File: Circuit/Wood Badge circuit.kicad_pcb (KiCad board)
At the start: 2 copper layers, 60 x 60 mm, 12 parts, among them J1 Conn_01x02_Pin, U1 LM555xN

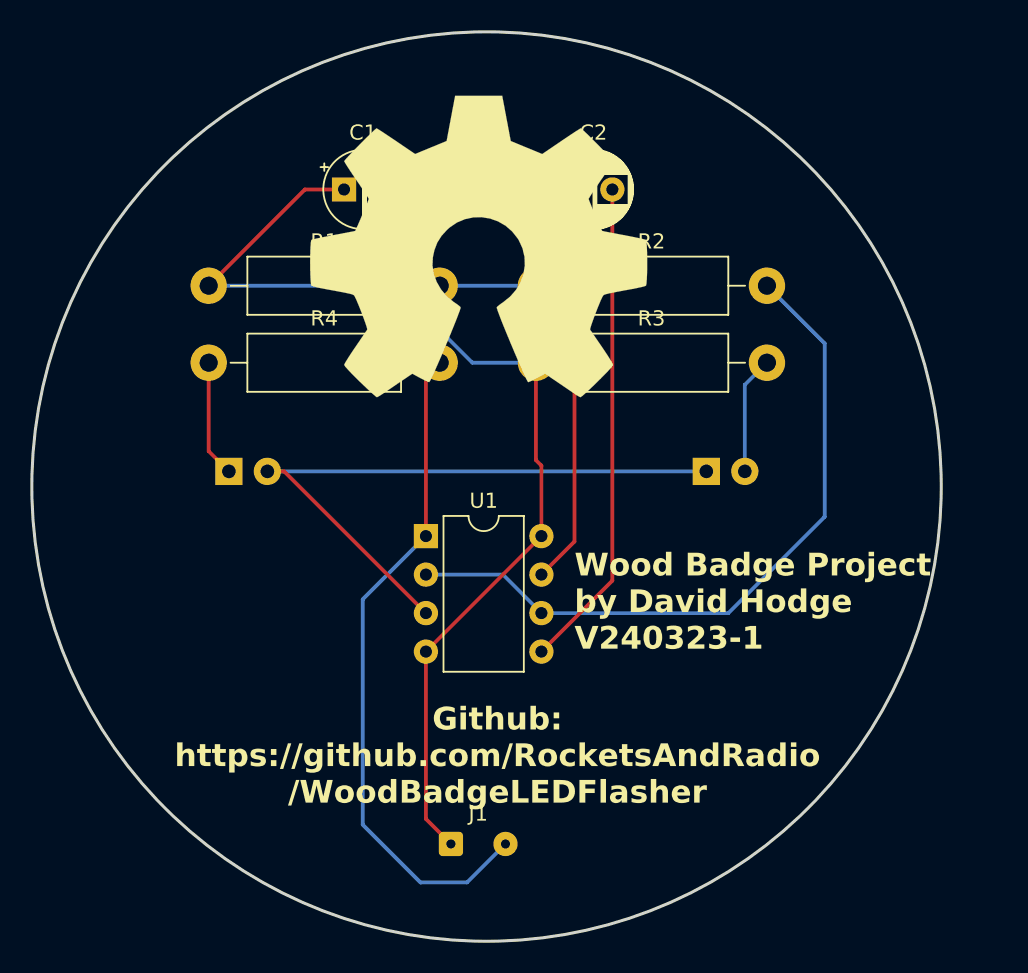
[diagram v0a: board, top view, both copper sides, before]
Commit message: Added C3 (below R1, R2 oops) Added values of components to reach a 2Hz frequency
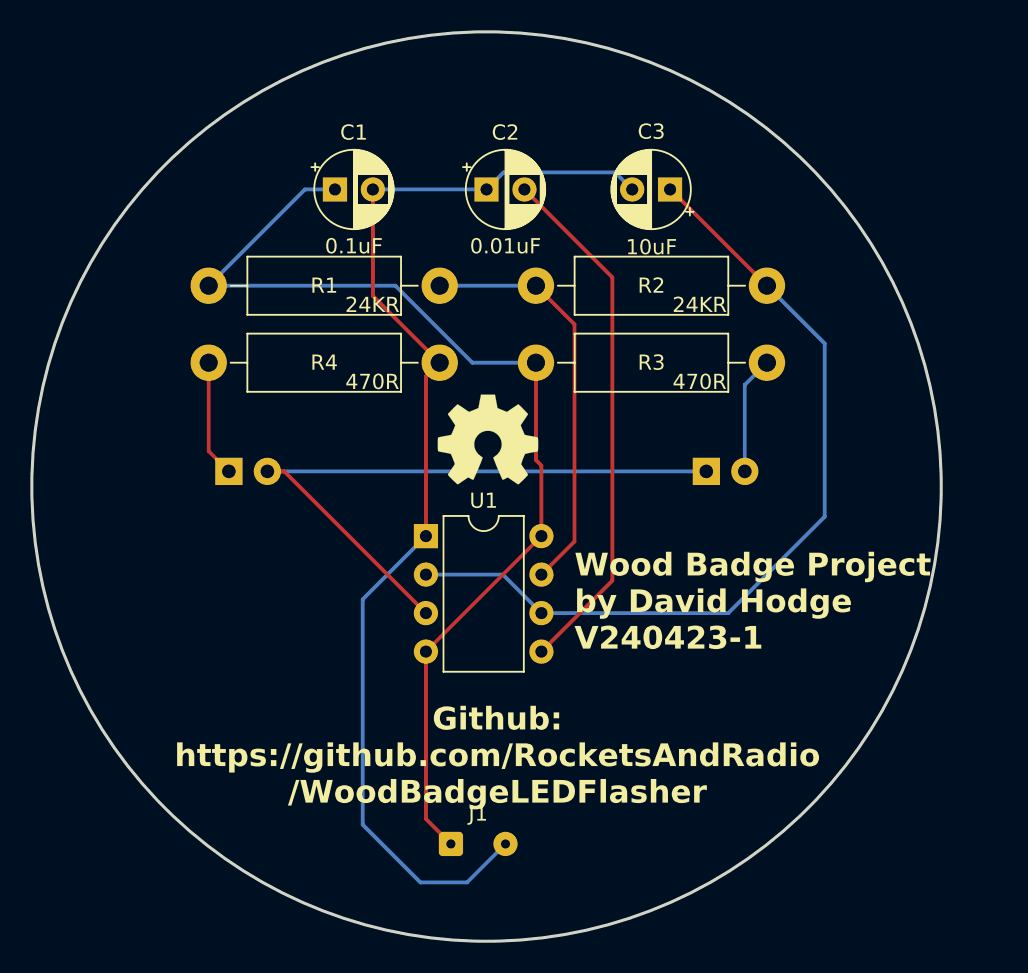
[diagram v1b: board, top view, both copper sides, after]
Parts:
- removed the REF** at (44.5, 29.2)
- added C3: 10uF, Capacitor_THT:CP_Radial_D5.0mm_P2.50mm, F.Cu at (57.1, 25.4)
- added REF**: OSHW-Symbol_6.7x6mm_SilkScreen, Symbol:OSHW-Symbol_6.7x6mm_SilkScreen, F.Cu at (45.1, 41.9)
- C1: value C_Small -> 0.1uF
- C2: value C_Small -> 0.01uF
- R1, R2: value R_US -> 24KR
- R3, R4: value R_US -> 470R
- moved C2 5.80 mm to (45.0, 25.4)
- moved C1 0.60 mm to (35.0, 25.4)
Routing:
- net /trigger-threshold: track 46.8 -> 55.8 mm
- net GND: track 70.3 -> 75.9 mm
- net Net-(U1-CV): track 32.4 -> 34.8 mm
- net VCC: track 71.0 -> 70.4 mm
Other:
- board text added: "Wood Badge Project by David Hodge V240423-1"
- board text removed: "Wood Badge Project by David Hodge V240323-1"

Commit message: Amendments to reflect fixes for faults identified in the first time the circuit was put together, such as adding capacitor C3.
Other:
- board text added: "Wood Badge Project by Kanga V240517-1"
- board text removed: "Wood Badge Project by David Hodge V240423-1"
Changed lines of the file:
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@@
 		(pad "1" thru_hole rect
 			(at 0 0)
-			(size 1.6 1.6)
+			(size 2 2.5)
 			(drill 0.8)
 			(layers "*.Cu" "*.Mask")
@@
 		(pad "2" thru_hole circle
 			(at 2.5 0)
-			(size 1.6 1.6)
+			(size 2 2)
 			(drill 0.8)
 			(layers "*.Cu" "*.Mask")
@@
 		(pad "1" thru_hole rect
 			(at 0 0)
-			(size 1.6 1.6)
+			(size 2.5 2)
 			(drill 0.8)
 			(layers "*.Cu" "*.Mask")
@@
 		(pad "2" thru_hole oval
 			(at 0 2.54)
-			(size 1.6 1.6)
+			(size 2 2)
 			(drill 0.8)
 			(layers "*.Cu" "*.Mask")
@@
 		(pad "3" thru_hole oval
 			(at 0 5.08)
-			(size 1.6 1.6)
+			(size 2 2)
 			(drill 0.8)
 			(layers "*.Cu" "*.Mask")
@@
 		(pad "4" thru_hole oval
 			(at 0 7.62)
-			(size 1.6 1.6)
+			(size 2 2)
 			(drill 0.8)
 			(layers "*.Cu" "*.Mask")
@@
 		(pad "5" thru_hole oval
 			(at 7.62 7.62)
-			(size 1.6 1.6)
+			(size 2 2)
 			(drill 0.8)
 			(layers "*.Cu" "*.Mask")
@@
 		(pad "6" thru_hole oval
 			(at 7.62 5.08)
-			(size 1.6 1.6)
+			(size 2 2)
 			(drill 0.8)
 			(layers "*.Cu" "*.Mask")
@@
 		(pad "7" thru_hole oval
 			(at 7.62 2.54)
-			(size 1.6 1.6)
+			(size 2 2)
 			(drill 0.8)
 			(layers "*.Cu" "*.Mask")
@@
 		(pad "8" thru_hole oval
 			(at 7.62 0)
-			(size 1.6 1.6)
+			(size 2 2)
 			(drill 0.8)
 			(layers "*.Cu" "*.Mask")
@@
 		(pad "1" thru_hole rect
 			(at 0 0)
-			(size 1.6 1.6)
+			(size 2 2.5)
 			(drill 0.8)
 			(layers "*.Cu" "*.Mask")
@@
 		(pad "2" thru_hole circle
 			(at 2.5 0)
-			(size 1.6 1.6)
+			(size 2 2)
 			(drill 0.8)
 			(layers "*.Cu" "*.Mask")
@@
 		(pad "1" thru_hole rect
 			(at 0 0 180)
-			(size 1.6 1.6)
+			(size 2 2.5)
 			(drill 0.8)
 			(layers "*.Cu" "*.Mask")
@@
 		(pad "2" thru_hole circle
 			(at 2.5 0 180)
-			(size 1.6 1.6)
+			(size 2 2)
 			(drill 0.8)
 			(layers "*.Cu" "*.Mask")
@@
 		(tags "connector wire 0.1sqmm")
 		(property "Reference" "J1"
-			(at 1.8 -2 0)
+			(at 1.8 1.905 0)
 			(layer "F.SilkS")
 			(effects
@@
 		(pad "1" thru_hole roundrect
 			(at 0 0)
-			(size 1.6 1.6)
-			(drill 0.6)
+			(size 2.5 2.5)
+			(drill 1)
 			(layers "*.Cu" "*.Mask")
 			(remove_unused_layers no)
@@
 		(pad "2" thru_hole circle
 			(at 3.6 0)
-			(size 1.6 1.6)
-			(drill 0.6)
+			(size 2.5 2.5)
+			(drill 1)
 			(layers "*.Cu" "*.Mask")
 			(remove_unused_layers no)
@@
 		(pad "1" thru_hole rect
 			(at 0 0)
-			(size 1.8 1.8)
+			(size 2 2.5)
 			(drill 0.9)
 			(layers "*.Cu" "*.Mask")
@@
 		(pad "2" thru_hole circle
 			(at 2.54 0)
-			(size 1.8 1.8)
+			(size 2 2)
 			(drill 0.9)
 			(layers "*.Cu" "*.Mask")
@@
 		(pad "1" thru_hole rect
 			(at 0 0)
-			(size 1.8 1.8)
+			(size 2 2.5)
 			(drill 0.9)
 			(layers "*.Cu" "*.Mask")
@@
 		(pad "2" thru_hole circle
 			(at 2.54 0)
-			(size 1.8 1.8)
+			(size 2 2)
 			(drill 0.9)
 			(layers "*.Cu" "*.Mask")
@@
 		(layer "Edge.Cuts")
 	)
-	(gr_text "Wood Badge Project\nby David Hodge\nV240423-1"
-		(at 50.8 55.88 0)
+	(gr_text "Wood Badge \nProject\nby Kanga\nV240517-1"
+		(at 52.07 57.658 0)
 		(layer "F.SilkS")
 		(effects
@@
 	)
 	(segment
-		(start 46.125 24.275)
-		(end 53.485 24.275)
+		(start 46.25 68.58)
+		(end 43.71 71.12)
 		(width 0.25)
 		(layer "B.Cu")
@@
 	)
 	(segment
-		(start 53.485 24.275)
-		(end 54.61 25.4)
+		(start 40.64 71.12)
+		(end 36.83 67.31)
 		(width 0.25)
 		(layer "B.Cu")
@@
 	)
 	(segment
-		(start 46.25 68.58)
-		(end 43.71 71.12)
+		(start 53.285 24.075)
+		(end 54.61 25.4)
 		(width 0.25)
 		(layer "B.Cu")
@@
 	)
 	(segment
-		(start 40.64 71.12)
-		(end 36.83 67.31)
+		(start 36.83 67.31)
+		(end 36.83 52.44)
 		(width 0.25)
 		(layer "B.Cu")
@@
 	)
 	(segment
-		(start 45 25.4)
-		(end 46.125 24.275)
+		(start 46.325 24.075)
+		(end 53.285 24.075)
 		(width 0.25)
 		(layer "B.Cu")
@@
 	)
 	(segment
-		(start 36.83 67.31)
-		(end 36.83 52.44)
+		(start 45 25.4)
+		(end 46.325 24.075)
 		(width 0.25)
 		(layer "B.Cu")

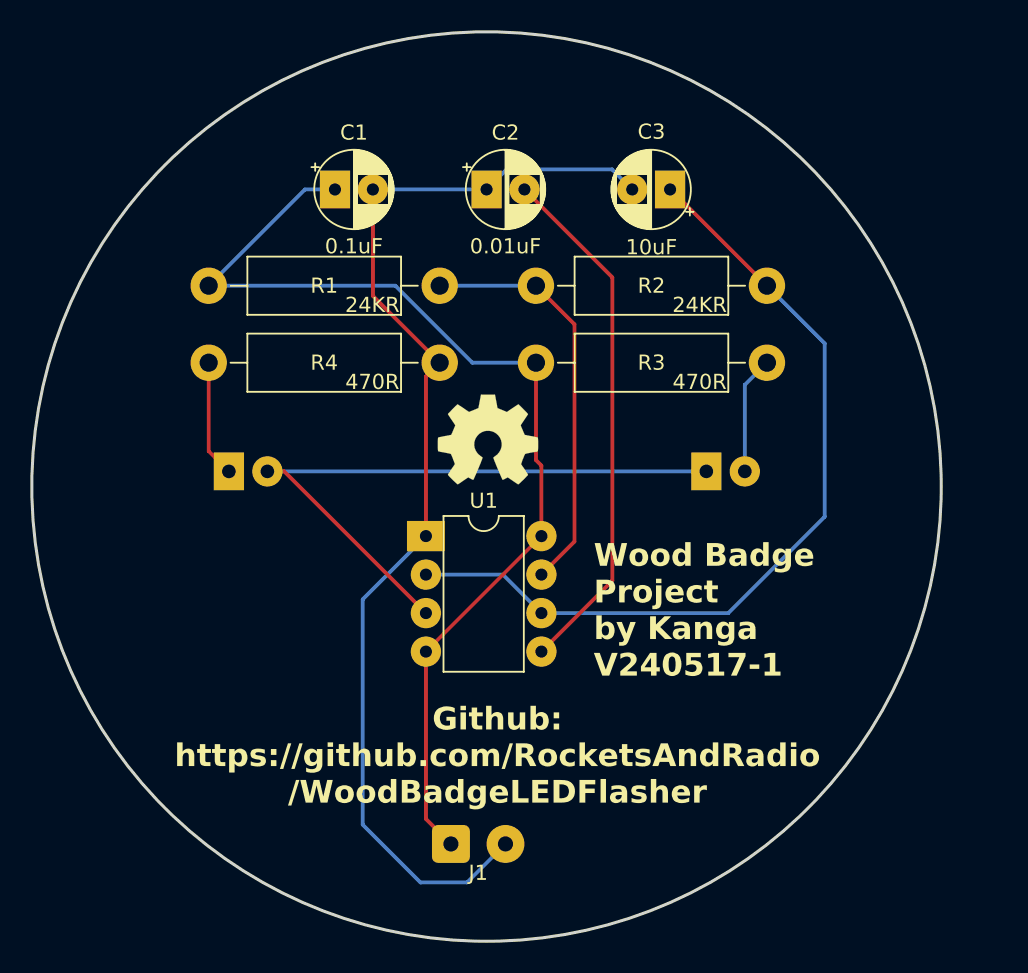
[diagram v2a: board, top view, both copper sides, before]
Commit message: Added: + and - on the solar panel connection LED outline to show where the 'flat edge' needs to go
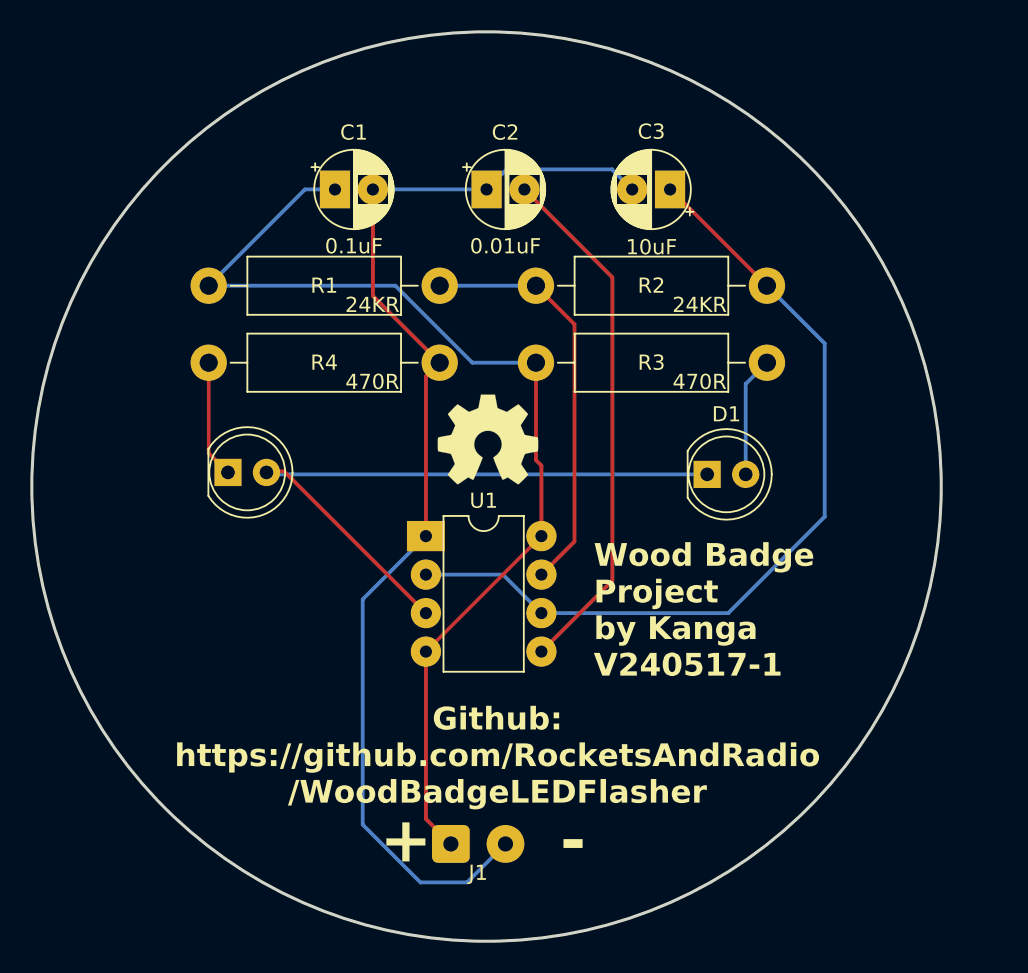
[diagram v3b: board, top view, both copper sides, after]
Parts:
- D1, D2: moved to F.Cu
- moved D1 0.20 mm to (59.6, 44.2)
- moved D2 0.09 mm to (27.9, 44.1)
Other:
- board text added: "+"
- board text added: "-"
